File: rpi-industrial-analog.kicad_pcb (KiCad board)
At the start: 2 copper layers, 100.1 x 50 mm, 68 parts, among them J101 CONN_01X04, J102 CONN_01X08, U101 MCP3424, U102 ICL7660S,A, U103 AD8220, U104 AD8220, U105 AD8220, U106 AD8220

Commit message: Layout complete
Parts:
- added LG101: 3ML_LOGO, 3ML_Footprint_Library:3ML_LOGO, F.Cu at (109.7, 88.4)
- moved TP107 260.9 mm to (177.4, 124.2)
- moved TP105 227.4 mm to (154.1, 121.4)
- moved TP104 209.7 mm to (131.7, 118.4)
- moved TP106 204.0 mm to (153.8, 111.5)
- moved R106 188.9 mm to (132.7, 84.6), turned to 180 degrees
- moved C113 187.9 mm to (135.4, 82.5)
- moved C117 186.0 mm to (159.1, 86.9), turned to 270 degrees
- moved C108 183.5 mm to (132.8, 89.8)
- moved C102 182.7 mm to (112.6, 96.6), turned to 180 degrees
- moved C112 181.7 mm to (136.5, 93.2)
- moved C109 181.6 mm to (131.3, 81.2)
- moved C103 180.4 mm to (112.6, 99.6), turned to 180 degrees
- moved R110 177.3 mm to (154.1, 85.9), turned to 180 degrees
- moved R101 176.6 mm to (112.5, 103.1), turned to 180 degrees
- moved C111 176.5 mm to (135.9, 102.9)
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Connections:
- J102 pad 5: (no net) -> /AIN3+
- J102 pad 6: (no net) -> /AIN3-
- J102 pad 7: (no net) -> /AIN4+
- J102 pad 8: (no net) -> /AIN4-
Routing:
- net +5V: track 0.00 -> 182.5 mm, vias 0 -> 5
- net -5V: track 0.00 -> 102.4 mm, vias 0 -> 5
- net /AIN1-: track 0.00 -> 69.1 mm
- net /AIN4-: track 0.00 -> 56.7 mm
- net /AIN2-: track 0.00 -> 56.7 mm
- net /AIN3-: track 0.00 -> 56.6 mm
- net GND: track 0.00 -> 38.3 mm, vias 0 -> 2
- net /AIN1+: track 0.00 -> 37.5 mm
- net /CH1+: track 0.00 -> 31.1 mm
- net Net-(C114-Pad1): track 0.00 -> 30.2 mm
- net /AIN4+: track 0.00 -> 30.0 mm
- net /AIN3+: track 0.00 -> 29.7 mm
- net /AIN2+: track 0.00 -> 28.8 mm
- net Net-(C117-Pad1): track 0.00 -> 25.7 mm
- net Net-(C116-Pad1): track 0.00 -> 25.7 mm
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- added copper zone on B.Cu, net GND
- added copper zone on F.Cu, net GND
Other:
- board size 100.1 x 50 mm -> 88.4 x 50 mm
- net class Default: clearance 0.2 -> 0.1524; trace_width 0.25 -> 0.1524; via_dia 0.6 -> 0.6858; via_drill 0.4 -> 0.3302
- rule pad_to_mask_clearance: 0.2 -> 0.0254
- rule trace_clearance: 0.2 -> 0.1524
- rule trace_min: 0.2 -> 0.1524
- rule via_min_drill: 0.3 -> 0.3302
- rule via_min_size: 0.4 -> 0.6858
- board text added: "&"
- board text added: "0-10V"
- board text added: "1"
- board text added: "2"
- board text added: "2:"
- board text added: "3:"
- board text added: "4-20mA"
- board text added: "5V"
- board text added: "Analog In 1 ->"
- board text added: "Analog In 2 ->"
- board text added: "Analog In 3 ->"
- board text added: "Analog In 4 ->"
- board text added: "Analog Persistence v1.0"
- board text added: "GND"
- board text added: "SCL"
- board text added: "SDA"
- board text added: "|"

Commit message: adding logos and mounting holes
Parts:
- added ACC101: ACC_?, Mounting_Holes:MountingHole_3.2mm_M3_DIN965, F.Cu at (109.7, 123.7)
- added ACC102: ACC_?, Symbols:OSHW-Logo_5.7x6mm_SilkScreen, F.Cu at (126.0, 90.9)
- added ACC103: ACC_?, Mounting_Holes:MountingHole_3.2mm_M3_DIN965, F.Cu at (181.6, 81.8)
- added ACC104: ACC_?, Mounting_Holes:MountingHole_3.2mm_M3_DIN965, F.Cu at (181.9, 124.7)
- added ACC105: ACC_?, Mounting_Holes:MountingHole_3.2mm_M3_DIN965, F.Cu at (118.6, 81.8)

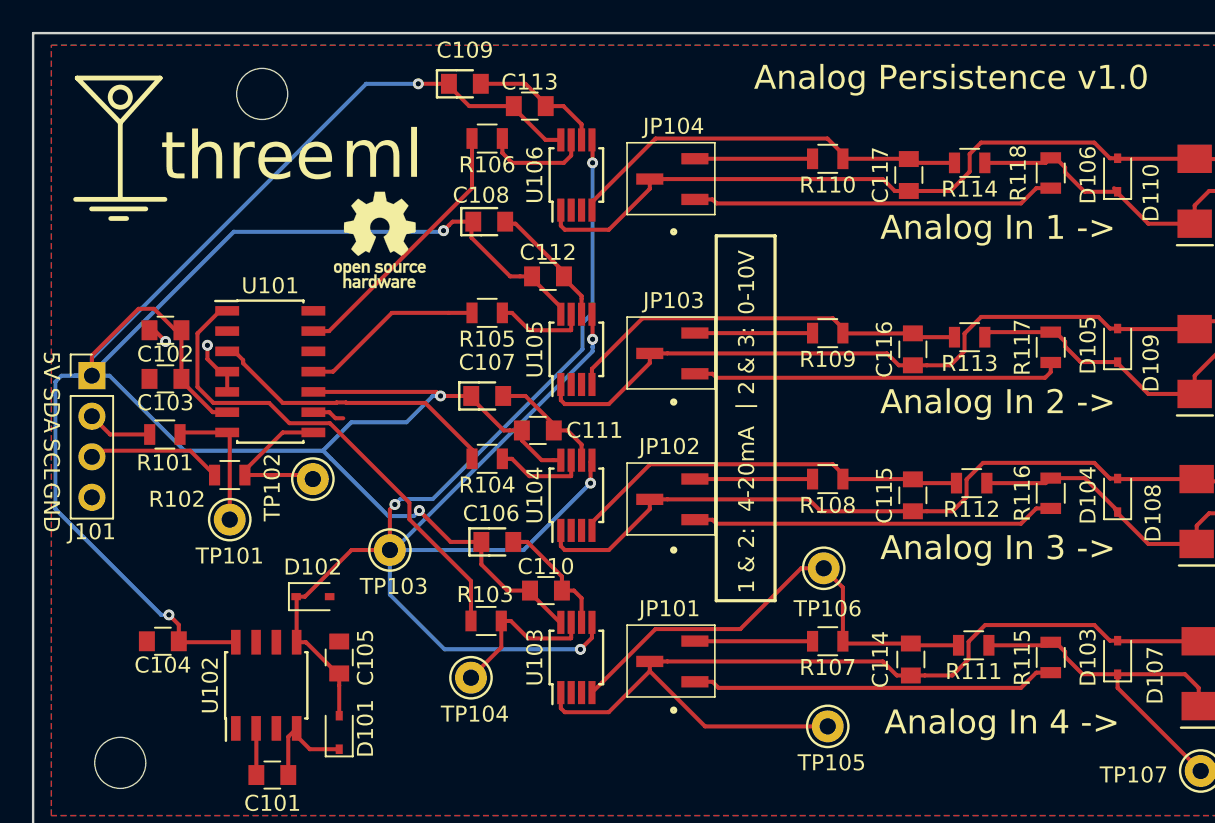
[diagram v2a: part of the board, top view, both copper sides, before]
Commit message: fixing some routing errors
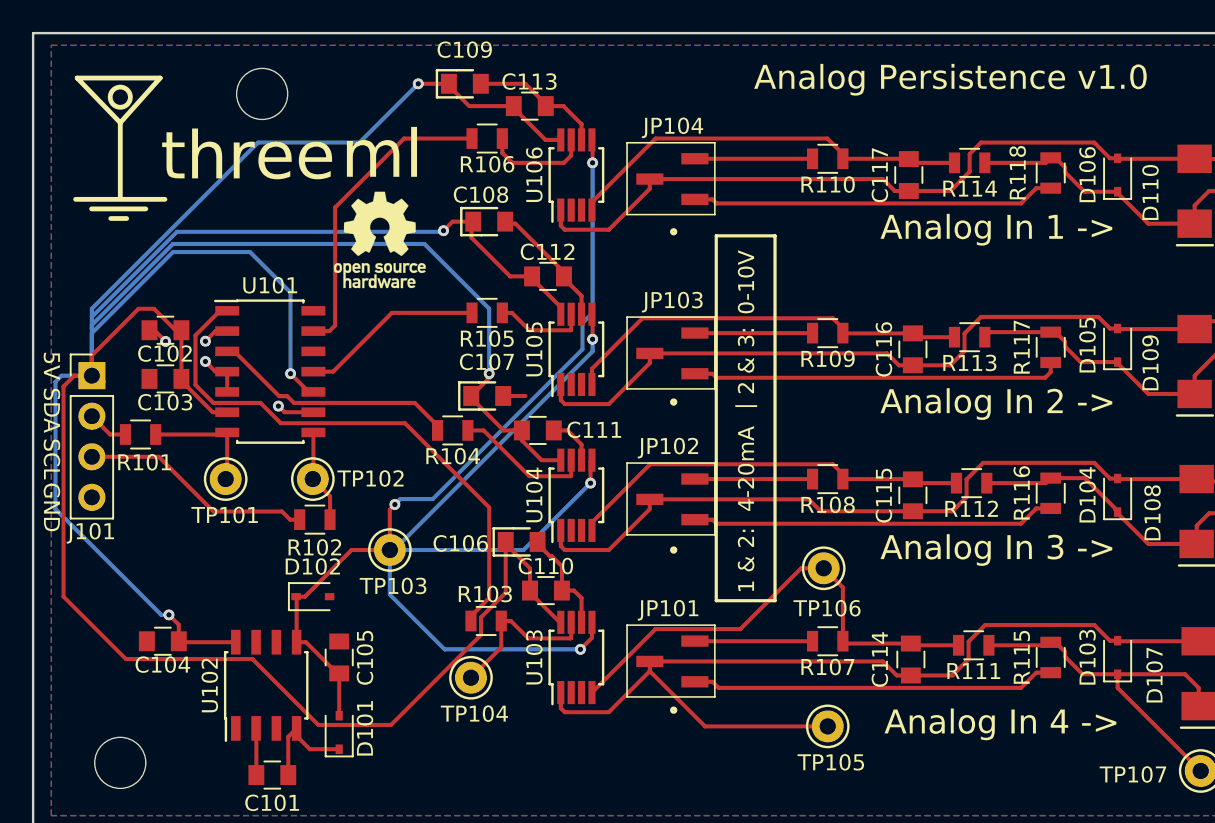
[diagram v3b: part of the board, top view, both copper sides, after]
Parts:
- moved R102 6.02 mm to (121.9, 108.5)
- moved R104 2.80 mm to (130.6, 102.9)
- moved TP101 2.55 mm to (116.3, 105.9)
- moved C106 1.52 mm to (134.9, 109.9)
- moved R101 1.52 mm to (111.0, 103.1)
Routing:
- net +5V: track 182.5 -> 251.1 mm
- net /SCL: track 8.48 -> 15.2 mm
- net /CH1+: track 31.1 -> 34.9 mm
- net Net-(R102-Pad2): track 10.4 -> 6.78 mm
- net /CH2+: track 19.0 -> 15.9 mm
- net Net-(R104-Pad1): track 5.75 -> 8.65 mm
- net /CH4+: track 16.8 -> 19.3 mm
- net GND: track 38.3 -> 36.3 mm, vias 2 -> 4
- net /SDA: track 4.10 -> 2.57 mm
- net Net-(R101-Pad1): track 8.53 -> 7.94 mm
